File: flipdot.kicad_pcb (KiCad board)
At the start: 2 copper layers, 121.3 x 14.6 mm, 43 parts, among them J1 Conn_01x06_Pin, U1 74HC595

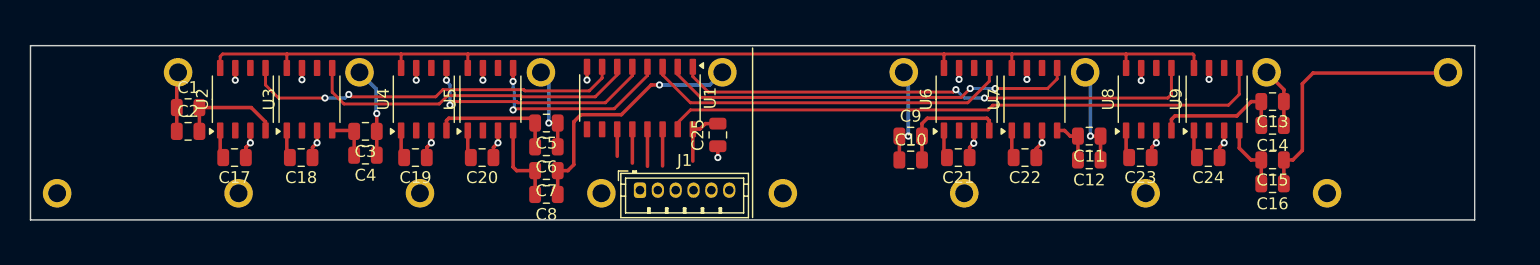
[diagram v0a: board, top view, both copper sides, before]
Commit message: use JST ZH
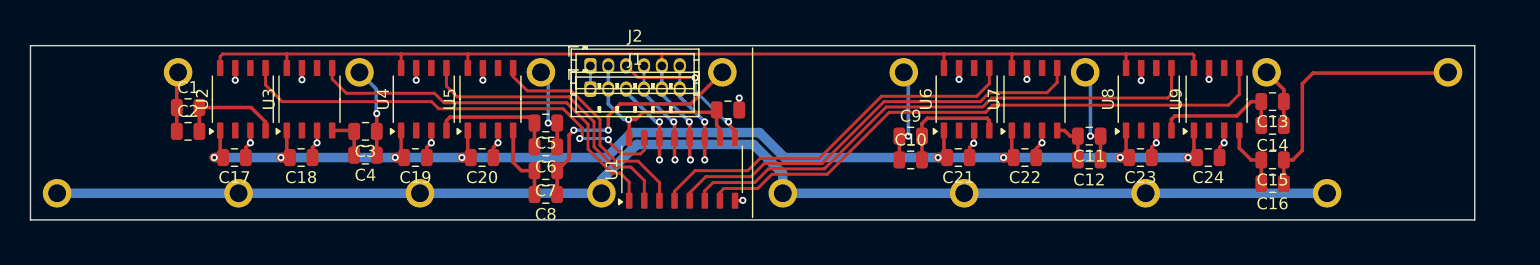
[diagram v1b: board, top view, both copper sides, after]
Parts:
- added J1: Conn_01x06_Pin, Connector_JST:JST_ZH_B6B-ZR_1x06_P1.50mm_Vertical, F.Cu at (44.8, -8.75)
- moved J2 11.2 mm to (44.8, -10.7)
- moved U1 6.97 mm to (52.5, -2.00), turned to 90 degrees
- moved C25 2.27 mm to (56.4, -7.00), turned to 180 degrees
- moved C5 0.05 mm to (41.0, -5.90)
- moved C6 0.05 mm to (41.0, -3.90)
- moved C7 0.05 mm to (41.0, -1.90)
- moved C8 0.05 mm to (41.0, 0.10)
- renumbered J1 to J2
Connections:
- J2 pad 3: /OE* -> /DATA_OUT
- J2 pad 4: /DATA_IN -> /OE*
- U2 pad 5: Net-(U1-QH) -> Net-(U1-QA)
- U3 pad 5: Net-(U1-QG) -> Net-(U1-QB)
- U4 pad 5: Net-(U1-QF) -> Net-(U1-QC)
- U5 pad 5: Net-(U1-QE) -> Net-(U1-QD)
- U6 pad 5: Net-(U1-QD) -> Net-(U1-QE)
- U7 pad 5: Net-(U1-QC) -> Net-(U1-QF)
- U8 pad 5: Net-(U1-QB) -> Net-(U1-QG)
- U9 pad 5: Net-(U1-QA) -> Net-(U1-QH)
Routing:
- net GND: track 29.6 -> 142.8 mm
- net +12V: track 19.1 -> 108.7 mm, vias 0 -> 8
- net Net-(U1-QH): track 32.0 -> 50.0 mm, vias 2 -> 0
- net Net-(U1-QG): track 28.2 -> 45.6 mm
- net Net-(U1-QF): track 20.4 -> 36.6 mm, vias 2 -> 0
- net Net-(U1-QE): track 16.8 -> 32.3 mm, vias 2 -> 0
- net Net-(U1-QA): track 50.9 -> 37.7 mm, vias 0 -> 2
- net /DATA_OUT: track 0.00 -> 12.8 mm, vias 0 -> 2
- net VCC: track 4.97 -> 17.3 mm, vias 0 -> 1
- net Net-(U1-QB): track 44.3 -> 32.3 mm, vias 2 -> 0
- net Net-(U1-QD): track 31.0 -> 19.5 mm
- net Net-(U1-QC): track 34.9 -> 24.4 mm, vias 2 -> 0
- net /LATCH: track 93.9 -> 100.9 mm, vias 0 -> 2
- net /CLK: track 2.27 -> 8.77 mm, vias 0 -> 2
- net /OE*: track 3.11 -> 9.04 mm, vias 0 -> 2
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
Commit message: keepout in wrong place
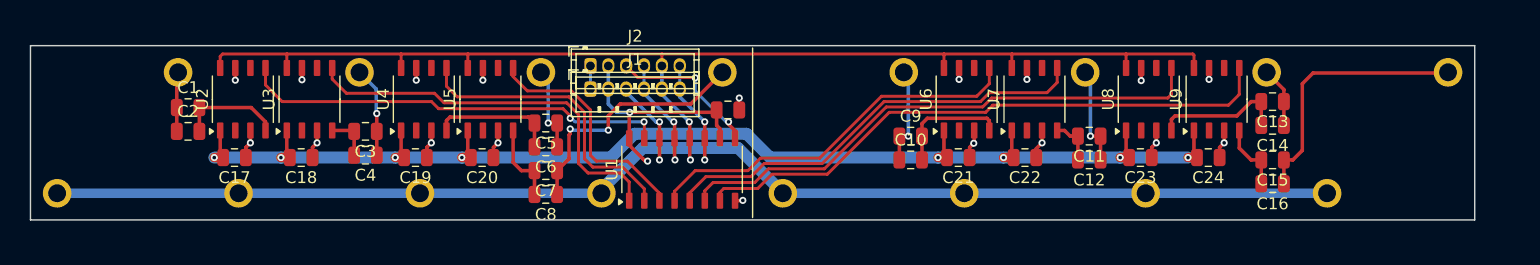
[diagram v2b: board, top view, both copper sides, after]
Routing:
- net VCC: track 17.3 -> 20.1 mm, vias 1 -> 2
- net GND: track 142.8 -> 141.2 mm
- net Net-(U1-QA): track 37.7 -> 36.0 mm
- net Net-(U1-QB): track 32.3 -> 33.4 mm
- net Net-(U1-QC): track 24.4 -> 25.0 mm

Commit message: flip everything again
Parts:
- moved J2 16.3 mm to (56.4, 0.70), turned to 180 degrees
- moved J1 13.8 mm to (56.4, -1.25), turned to 180 degrees
- moved U1 7.07 mm to (48.6, -7.90), turned to -90 degrees
- moved C25 1.86 mm to (55.9, -5.20)
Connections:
- U2 pad 5: Net-(U1-QA) -> Net-(U1-QH)
- U3 pad 5: Net-(U1-QB) -> Net-(U1-QG)
- U4 pad 5: Net-(U1-QC) -> Net-(U1-QF)
- U5 pad 5: Net-(U1-QD) -> Net-(U1-QE)
- U6 pad 5: Net-(U1-QE) -> Net-(U1-QD)
- U7 pad 5: Net-(U1-QF) -> Net-(U1-QC)
- U8 pad 5: Net-(U1-QG) -> Net-(U1-QB)
- U9 pad 5: Net-(U1-QH) -> Net-(U1-QA)
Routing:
- net Net-(U1-QG): track 45.6 -> 26.8 mm
- net Net-(U1-QH): track 50.0 -> 33.0 mm, vias 0 -> 2
- net Net-(U1-QA): track 36.0 -> 52.4 mm
- net Net-(L4-ROW): track 21.5 -> 5.41 mm, vias 2 -> 0
- net Net-(U1-QE): track 32.3 -> 16.3 mm, vias 0 -> 2
- net Net-(U1-QF): track 36.6 -> 20.7 mm, vias 0 -> 2
- net Net-(U1-QD): track 19.9 -> 33.6 mm, vias 0 -> 2
- net Net-(U1-QB): track 33.4 -> 45.3 mm, vias 0 -> 2
- net Net-(U1-QC): track 25.0 -> 35.2 mm
- net GND: track 141.2 -> 145.7 mm
- net /LATCH: track 100.9 -> 104.8 mm
- net /OE*: track 9.04 -> 12.6 mm, vias 2 -> 1
- net /CLK: track 8.77 -> 12.2 mm, vias 2 -> 1
- net /DATA_IN: track 7.29 -> 10.6 mm, vias 2 -> 1
- net VCC: track 20.1 -> 22.5 mm, vias 2 -> 1
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
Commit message: some progress
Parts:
- added J3: Conn_01x02_Pin, Connector_JST:JST_VH_B2P-VH_1x02_P3.96mm_Vertical, F.Cu at (8.70, -3.96)
- added J4: Conn_01x02_Pin, Connector_JST:JST_VH_B2P-VH_1x02_P3.96mm_Vertical, F.Cu at (65.8, -3.86)
- added J5: Conn_01x02_Pin, Connector_JST:JST_VH_B2P-VH_1x02_P3.96mm_Vertical, F.Cu at (108.4, -5.94)
- moved C2 7.22 mm to (5.60, -10.0), turned to -90 degrees
- moved C1 4.40 mm to (7.60, -10.0), turned to -90 degrees
- moved C17 0.20 mm to (15.1, -3.00)
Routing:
- net Net-(L4-ROW): track 5.41 -> 21.0 mm, vias 0 -> 1
- net Net-(U2-AOUT): track 8.77 -> 13.9 mm
- net +12V: track 107.8 -> 112.8 mm
- net /CLK: track 12.2 -> 14.0 mm
- net Net-(L8-ROW): track 22.1 -> 20.6 mm
- net /OE*: track 12.6 -> 14.0 mm
- net /DATA_IN: track 10.6 -> 12.0 mm
- net VCC: track 22.5 -> 23.7 mm
- net Net-(U1-QB): track 45.3 -> 46.0 mm
- added copper zone on B.Cu, net GND
- added copper zone on F.Cu, net GND

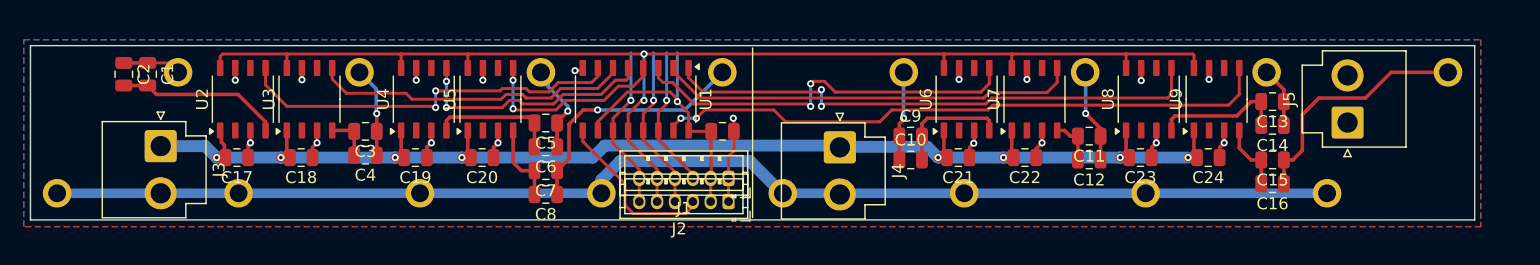
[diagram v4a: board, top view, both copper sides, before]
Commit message: mounting holes
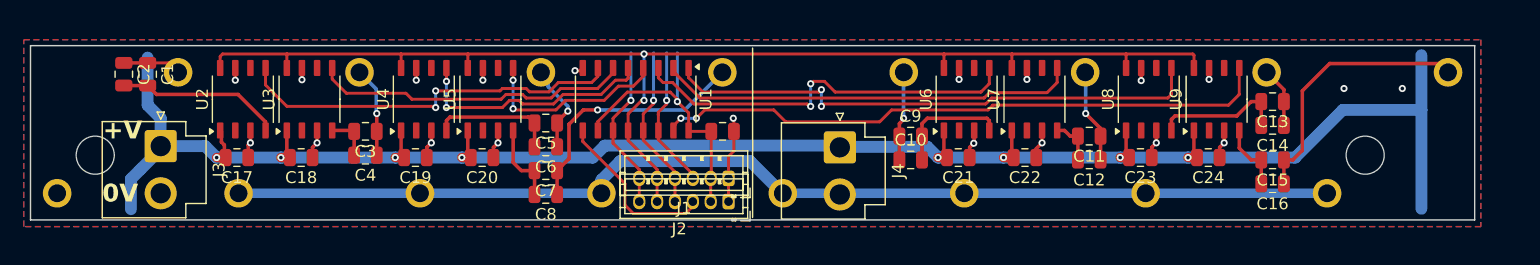
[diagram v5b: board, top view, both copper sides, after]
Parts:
- removed J5: Conn_01x02_Pin, Connector_JST:JST_VH_B2P-VH_1x02_P3.96mm_Vertical
- added REF**: MountingHole_3.2mm_M3_DIN965, MountingHole:MountingHole_3.2mm_M3_DIN965, F.Cu at (109.9, -3.20)
- added REF**: MountingHole_3.2mm_M3_DIN965, MountingHole:MountingHole_3.2mm_M3_DIN965, F.Cu at (3.20, -3.20)
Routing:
- net +12V: track 112.8 -> 161.2 mm
- net GND: track 145.6 -> 130.4 mm
- net Net-(L8-ROW): track 20.6 -> 22.4 mm
- net (no net): vias 0 -> 2
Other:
- board text added: "+V"
- board text added: "0V"

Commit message: fatten 12v line
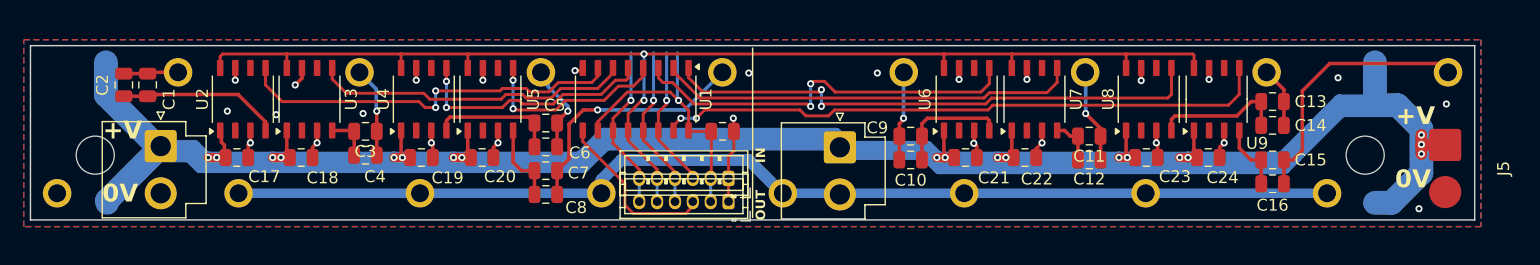
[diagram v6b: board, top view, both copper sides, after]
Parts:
- added J5: Conn_01x02_Pin, Connector_JST:JST_VH_B2P-VH_1x02_P3.96mm_Vertical, F.Cu at (116.6, -4.06)
- moved C1 0.90 mm to (7.60, -9.10)
- moved C2 0.90 mm to (5.60, -9.10)
- moved C21 0.60 mm to (76.3, -3.00)
- moved C19 0.50 mm to (30.6, -3.00)
- moved C23 0.50 mm to (91.5, -3.00)
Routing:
- net +12V: track 161.2 -> 282.9 mm, vias 8 -> 19
- net GND: track 130.4 -> 131.0 mm, vias 18 -> 26
- net (no net): vias 2 -> 0
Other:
- board text added: "IN"
- board text added: "OUT"

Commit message: single row mostly complete
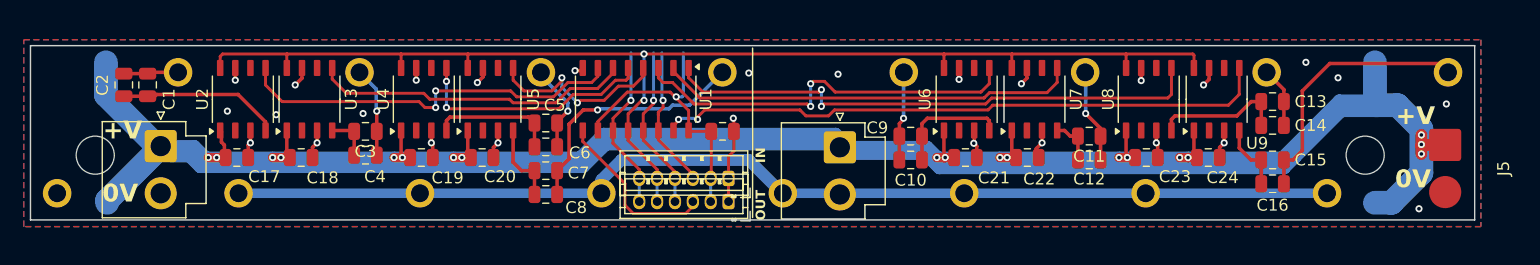
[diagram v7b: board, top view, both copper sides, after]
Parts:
- moved C22 0.20 mm to (81.5, -3.00)
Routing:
- net GND: track 131.0 -> 132.7 mm, vias 26 -> 27

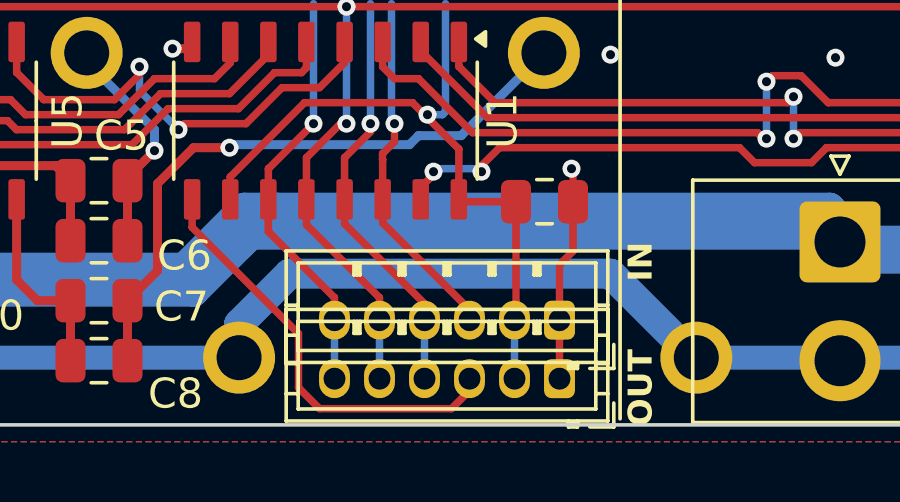
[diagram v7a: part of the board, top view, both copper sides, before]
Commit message: use single component for connector
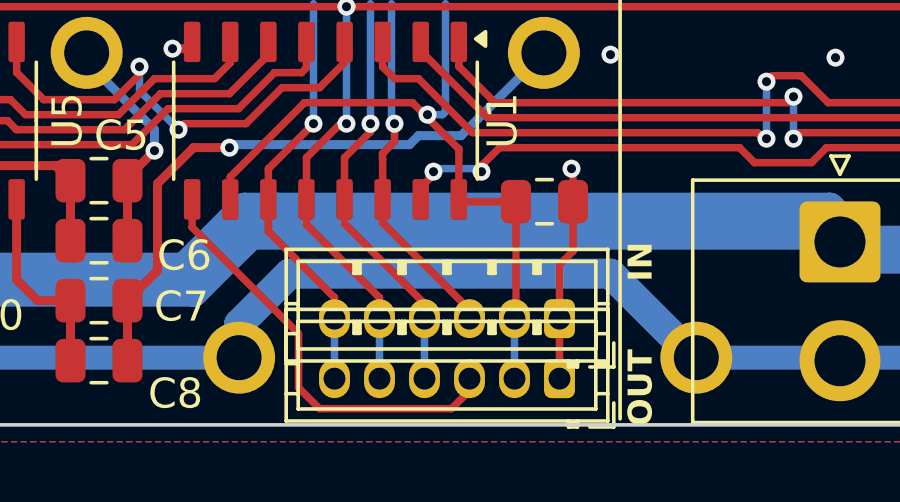
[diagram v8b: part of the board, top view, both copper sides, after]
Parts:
- removed J2: Conn_01x06_Pin, Connector_JST:JST_ZH_B6B-ZR_1x06_P1.50mm_Vertical
- H1, H2: renamed from REF**; value MountingHole_3.2mm_M3_DIN965 -> MountingHole
- J1: value Conn_01x06_Pin -> Conn_01x12_Pin
- moved J1 1.95 mm to (56.4, 0.70)
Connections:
- J1 pad 3: /DATA_IN -> /DATA_OUT
